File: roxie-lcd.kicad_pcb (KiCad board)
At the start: 2 copper layers, 7 parts, among them J1 Arduino-NANO-33, J2 VESC, J3 TFT, J4 BUTTON_1, J5 BUTTON_2, J6 BUTTON_3, J7 SD

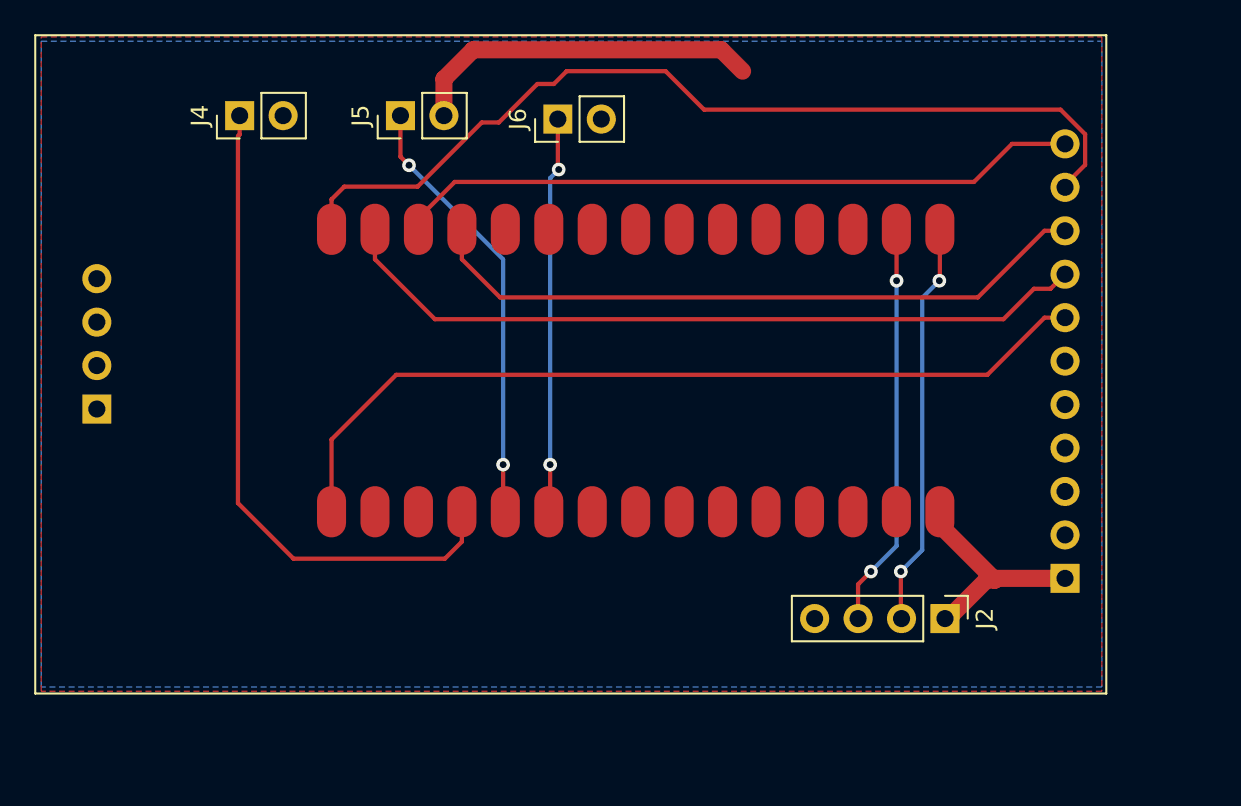
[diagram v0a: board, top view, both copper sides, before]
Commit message: changed button position
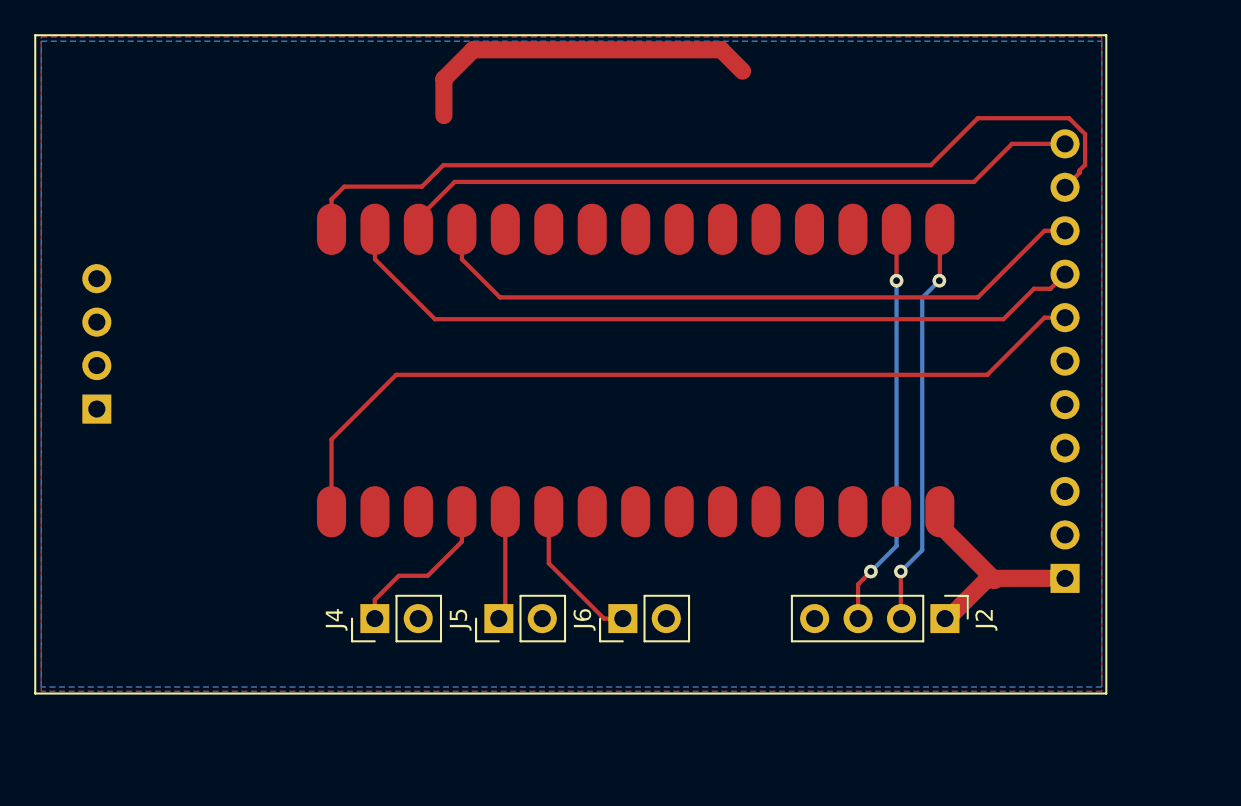
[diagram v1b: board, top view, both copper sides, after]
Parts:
- moved J4 30.4 mm to (45.2, 59.5)
- moved J5 30.0 mm to (52.5, 59.5)
- moved J6 29.4 mm to (59.8, 59.5)
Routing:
- net BUTTON_1: track 39.3 -> 9.35 mm
- net BUTTON_2: track 25.7 -> 6.40 mm, vias 2 -> 0
- net BUTTON_3: track 23.2 -> 8.68 mm, vias 2 -> 0
- net RST: track 54.2 -> 51.7 mm
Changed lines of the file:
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@@
     (thickness 1.6)
     (drawings 4)
-    (tracks 88)
+    (tracks 72)
     (zones 0)
     (modules 7)
@@
   )
   (setup
-    (last_trace_width 1)
+    (last_trace_width 0.25)
     (user_trace_width 1)
     (trace_clearance 0.2)
@@
   )
   (module Connector_PinHeader_2.54mm:PinHeader_1x02_P2.54mm_Vertical (layer F.Cu)
-    (at 55.95 30.3 90)
+    (at 59.75 59.5 90)
     (descr "Through hole straight pin header, 1x02, 2.54mm pitch, single row")
     (tags "Through hole pin header THT 1x02 2.54mm single row")
@@
   )
   (module Connector_PinHeader_2.54mm:PinHeader_1x02_P2.54mm_Vertical (layer F.Cu)
-    (at 46.75 30.1 90)
+    (at 52.5 59.5 90)
     (descr "Through hole straight pin header, 1x02, 2.54mm pitch, single row")
     (tags "Through hole pin header THT 1x02 2.54mm single row")
@@
   )
   (module Connector_PinHeader_2.54mm:PinHeader_1x02_P2.54mm_Vertical (layer F.Cu)
-    (at 37.35 30.1 90)
+    (at 45.25 59.5 90)
     (descr "Through hole straight pin header, 1x02, 2.54mm pitch, single row")
     (tags "Through hole pin header THT 1x02 2.54mm single row")
@@
   (segment (start 45.26 38.495) (end 45.26 36.745) (width 0.25) (layer F.Cu) (net 23))
   (segment (start 82 42) (end 48.765 42) (width 0.25) (layer F.Cu) (net 23))
-  (segment (start 85.598 34.29) (end 85.46 34.29) (width 0.25) (layer F.Cu) (net 24))
-  (segment (start 86.773001 31.185999) (end 85.337002 29.75) (width 0.25) (layer F.Cu) (net 24))
-  (segment (start 85.46 34.29) (end 86.773001 32.976999) (width 0.25) (layer F.Cu) (net 24))
+  (segment (start 86.447999 33.440001) (end 86.447999 33.302001) (width 0.25) (layer F.Cu) (net 24))
+  (segment (start 85.598 34.29) (end 86.447999 33.440001) (width 0.25) (layer F.Cu) (net 24))
+  (segment (start 86.773001 31.185999) (end 85.837002 30.25) (width 0.25) (layer F.Cu) (net 24))
+  (segment (start 86.447999 33.302001) (end 86.773001 32.976999) (width 0.25) (layer F.Cu) (net 24))
   (segment (start 86.773001 32.976999) (end 86.773001 31.185999) (width 0.25) (layer F.Cu) (net 24))
-  (segment (start 85.337002 29.75) (end 64.5 29.75) (width 0.25) (layer F.Cu) (net 24))
-  (segment (start 64.5 29.75) (end 62.25 27.5) (width 0.25) (layer F.Cu) (net 24))
-  (segment (start 56.464998 27.5) (end 55.714998 28.25) (width 0.25) (layer F.Cu) (net 24))
-  (segment (start 62.25 27.5) (end 56.464998 27.5) (width 0.25) (layer F.Cu) (net 24))
-  (segment (start 55.714998 28.25) (end 54.75 28.25) (width 0.25) (layer F.Cu) (net 24))
-  (segment (start 54.75 28.25) (end 52.5 30.5) (width 0.25) (layer F.Cu) (net 24))
-  (segment (start 52.5 30.5) (end 51.5 30.5) (width 0.25) (layer F.Cu) (net 24))
-  (segment (start 51.5 30.5) (end 47.75 34.25) (width 0.25) (layer F.Cu) (net 24))
+  (segment (start 85.837002 30.25) (end 80.5 30.25) (width 0.25) (layer F.Cu) (net 24))
+  (segment (start 80.5 30.25) (end 77.75 33) (width 0.25) (layer F.Cu) (net 24))
+  (segment (start 77.75 33) (end 49.25 33) (width 0.25) (layer F.Cu) (net 24))
+  (segment (start 49.25 33) (end 48 34.25) (width 0.25) (layer F.Cu) (net 24))
   (segment (start 43.465 34.25) (end 42.72 34.995) (width 0.25) (layer F.Cu) (net 24))
   (segment (start 42.72 34.995) (end 42.72 36.745) (width 0.25) (layer F.Cu) (net 24))
-  (segment (start 47.75 34.25) (end 43.465 34.25) (width 0.25) (layer F.Cu) (net 24))
+  (segment (start 48 34.25) (end 43.465 34.25) (width 0.25) (layer F.Cu) (net 24))
   (segment (start 78.28 53.255) (end 78.28 54.03) (width 1) (layer F.Cu) (net 25))
   (segment (start 78.28 54.03) (end 81.5 57.25) (width 1) (layer F.Cu) (net 25))
@@
   (segment (start 81 57.25) (end 81.5 57.25) (width 1) (layer F.Cu) (net 25))
   (segment (start 78.75 59.5) (end 81 57.25) (width 1) (layer F.Cu) (net 25))
-  (via (at 56 33.25) (size 0.8) (drill 0.4) (layers F.Cu B.Cu) (net 26))
-  (segment (start 55.95 30.3) (end 55.95 33.2) (width 0.25) (layer F.Cu) (net 26))
-  (segment (start 55.95 33.2) (end 56 33.25) (width 0.25) (layer F.Cu) (net 26))
-  (via (at 55.5 50.5) (size 0.8) (drill 0.4) (layers F.Cu B.Cu) (net 26))
-  (segment (start 56 33.25) (end 55.5 33.75) (width 0.25) (layer B.Cu) (net 26))
-  (segment (start 55.5 33.75) (end 55.5 50.5) (width 0.25) (layer B.Cu) (net 26))
-  (segment (start 55.5 53.175) (end 55.42 53.255) (width 0.25) (layer F.Cu) (net 26))
-  (segment (start 55.5 50.5) (end 55.5 53.175) (width 0.25) (layer F.Cu) (net 26))
-  (segment (start 50.34 55.005) (end 50.34 53.255) (width 0.25) (layer F.Cu) (net 27))
-  (segment (start 37.35 30.1) (end 37.35 31.2) (width 0.25) (layer F.Cu) (net 27))
-  (segment (start 49.345 56) (end 50.34 55.005) (width 0.25) (layer F.Cu) (net 27))
-  (segment (start 37.25 31.3) (end 37.25 52.75) (width 0.25) (layer F.Cu) (net 27))
-  (segment (start 37.25 52.75) (end 40.5 56) (width 0.25) (layer F.Cu) (net 27))
-  (segment (start 40.5 56) (end 49.345 56) (width 0.25) (layer F.Cu) (net 27))
-  (segment (start 37.35 31.2) (end 37.25 31.3) (width 0.25) (layer F.Cu) (net 27))
+  (segment (start 58.65 59.5) (end 59.75 59.5) (width 0.25) (layer F.Cu) (net 26))
+  (segment (start 55.42 56.27) (end 58.65 59.5) (width 0.25) (layer F.Cu) (net 26))
+  (segment (start 55.42 53.255) (end 55.42 56.27) (width 0.25) (layer F.Cu) (net 26))
+  (segment (start 50.34 55.005) (end 48.345 57) (width 0.25) (layer F.Cu) (net 27))
+  (segment (start 50.34 53.255) (end 50.34 55.005) (width 0.25) (layer F.Cu) (net 27))
+  (segment (start 45.25 58.4) (end 45.25 59.5) (width 0.25) (layer F.Cu) (net 27))
+  (segment (start 46.65 57) (end 45.25 58.4) (width 0.25) (layer F.Cu) (net 27))
+  (segment (start 48.345 57) (end 46.65 57) (width 0.25) (layer F.Cu) (net 27))
   (segment (start 66.75 27.5) (end 65.5 26.25) (width 1) (layer F.Cu) (net 28))
   (segment (start 65.5 26.25) (end 51 26.25) (width 1) (layer F.Cu) (net 28))
@@
   (segment (start 42.72 49.03) (end 42.72 53.255) (width 0.25) (layer F.Cu) (net 29))
   (segment (start 46.5 45.25) (end 42.72 49.03) (width 0.25) (layer F.Cu) (net 29))
-  (segment (start 46.75 30.1) (end 46.75 32.5) (width 0.25) (layer F.Cu) (net 30))
-  (via (at 47.25 33) (size 0.8) (drill 0.4) (layers F.Cu B.Cu) (net 30))
-  (segment (start 46.75 32.5) (end 47.25 33) (width 0.25) (layer F.Cu) (net 30))
-  (via (at 52.75 50.5) (size 0.8) (drill 0.4) (layers F.Cu B.Cu) (net 30))
-  (segment (start 47.25 33) (end 52.75 38.5) (width 0.25) (layer B.Cu) (net 30))
-  (segment (start 52.75 38.5) (end 52.75 50.5) (width 0.25) (layer B.Cu) (net 30))
-  (segment (start 52.75 53.125) (end 52.88 53.255) (width 0.25) (layer F.Cu) (net 30))
-  (segment (start 52.75 50.5) (end 52.75 53.125) (width 0.25) (layer F.Cu) (net 30))
+  (segment (start 52.88 59.12) (end 52.5 59.5) (width 0.25) (layer F.Cu) (net 30))
+  (segment (start 52.88 53.255) (end 52.88 59.12) (width 0.25) (layer F.Cu) (net 30))
   (zone (net 28) (net_name GND) (layer F.Cu) (hatch edge 0.508)
     (connect_pads (clearance 0.508))

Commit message: changed some positions
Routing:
- net TX: track 23.7 -> 23.8 mm, vias 2 -> 1
- net RX: vias 2 -> 1
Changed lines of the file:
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@@
     (thickness 1.6)
     (drawings 4)
-    (tracks 72)
+    (tracks 69)
     (zones 0)
     (modules 7)
@@
   (segment (start 77.25 40.75) (end 77.25 55.5) (width 0.25) (layer B.Cu) (net 19))
   (segment (start 77.25 55.5) (end 76.04 56.71) (width 0.25) (layer B.Cu) (net 19))
-  (via (at 76 56.75) (size 0.8) (drill 0.4) (layers F.Cu B.Cu) (net 19))
   (segment (start 76.04 56.71) (end 76 56.75) (width 0.25) (layer B.Cu) (net 19))
   (segment (start 76 59.46) (end 76.04 59.5) (width 0.25) (layer F.Cu) (net 19))
-  (segment (start 76 56.75) (end 76 59.46) (width 0.25) (layer F.Cu) (net 19))
-  (via (at 74.25 56.75) (size 0.8) (drill 0.4) (layers F.Cu B.Cu) (net 20))
-  (segment (start 73.5 59.5) (end 73.5 57.5) (width 0.25) (layer F.Cu) (net 20))
-  (segment (start 73.5 57.5) (end 74.25 56.75) (width 0.25) (layer F.Cu) (net 20))
+  (segment (start 76.04 56.71) (end 76.04 59.5) (width 0.25) (layer B.Cu) (net 19))
   (via (at 75.75 39.75) (size 0.8) (drill 0.4) (layers F.Cu B.Cu) (net 20))
-  (segment (start 74.25 56.75) (end 75.75 55.25) (width 0.25) (layer B.Cu) (net 20))
-  (segment (start 75.75 55.25) (end 75.75 39.75) (width 0.25) (layer B.Cu) (net 20))
   (segment (start 75.75 36.755) (end 75.74 36.745) (width 0.25) (layer F.Cu) (net 20))
   (segment (start 75.75 39.75) (end 75.75 36.755) (width 0.25) (layer F.Cu) (net 20))
+  (segment (start 75.75 39.75) (end 75.75 55.25) (width 0.25) (layer B.Cu) (net 20))
+  (segment (start 73.5 57.5) (end 73.5 59.5) (width 0.25) (layer B.Cu) (net 20))
+  (segment (start 75.75 55.25) (end 73.5 57.5) (width 0.25) (layer B.Cu) (net 20))
   (segment (start 50.34 38.495) (end 50.34 36.745) (width 0.25) (layer F.Cu) (net 21))
   (segment (start 80.500918 40.725001) (end 52.570001 40.725001) (width 0.25) (layer F.Cu) (net 21))

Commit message: pcb designed
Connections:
- J1 pad 26: Net-(J1-Pad26) -> CS
- J1 pad 28: CS -> Net-(J1-Pad28)
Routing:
- net GND: track 20.8 -> 0.00 mm
- net CS: track 40.2 -> 35.2 mm
- net RST: track 51.7 -> 52.4 mm

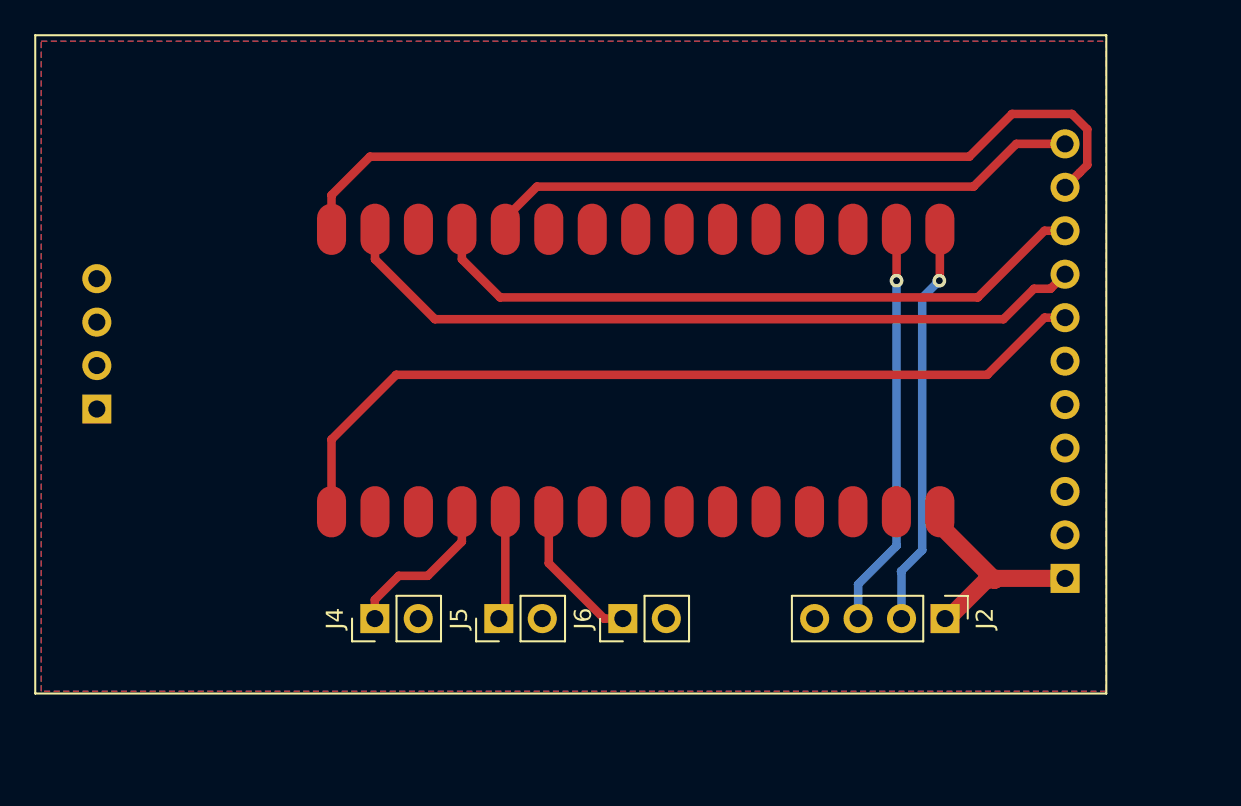
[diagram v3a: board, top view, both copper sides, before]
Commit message: changed position of connectors
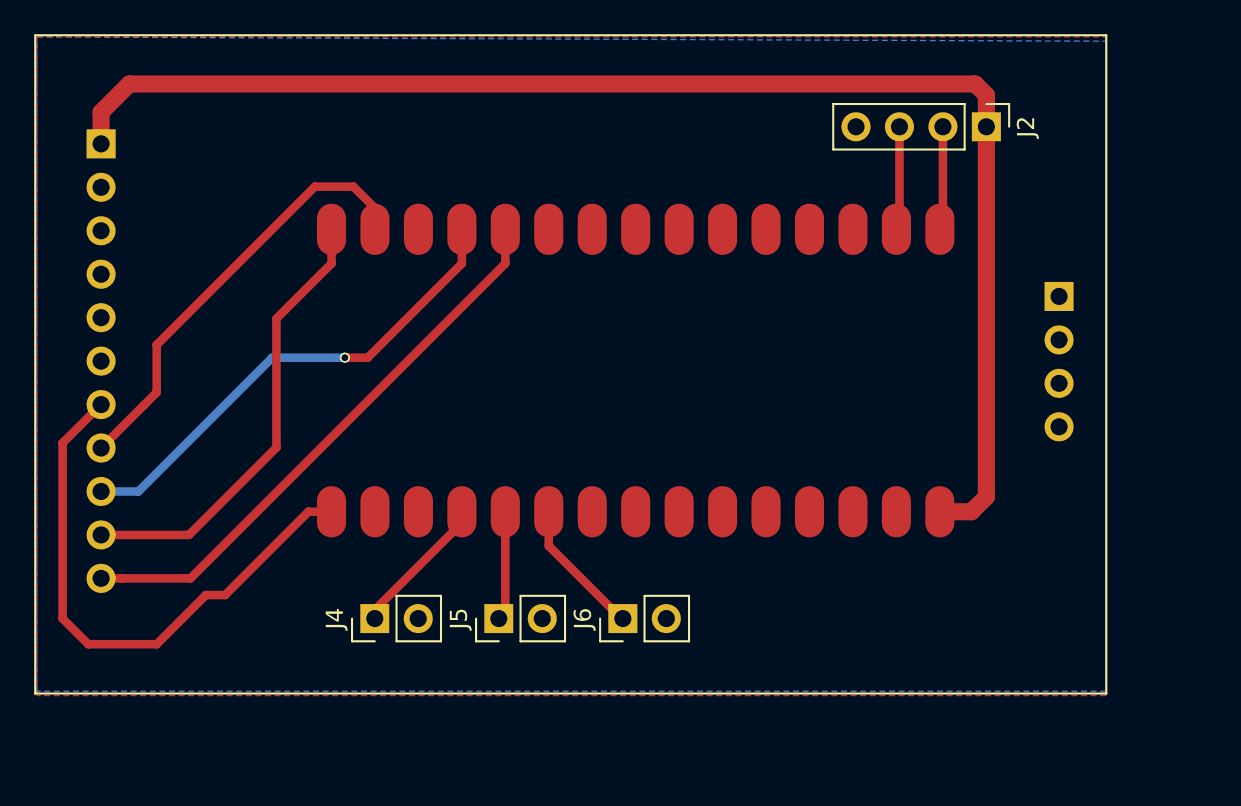
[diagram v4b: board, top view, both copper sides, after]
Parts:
- moved J3 61.8 mm to (29.2, 31.8), turned to 180 degrees
- moved J7 56.6 mm to (85.2, 40.7), turned to 180 degrees
- moved J2 28.9 mm to (81.0, 30.8)
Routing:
- net 5V: track 13.3 -> 81.1 mm
- net RST: track 52.4 -> 26.5 mm
- net SDA: track 44.6 -> 25.7 mm
- net TX: track 23.8 -> 6.07 mm, vias 1 -> 0
- net RX: track 23.7 -> 6.07 mm, vias 1 -> 0
- net CLK: track 50.1 -> 33.0 mm
- net RS: track 39.5 -> 28.6 mm, vias 0 -> 1
- net CS: track 35.2 -> 33.3 mm
- net BUTTON_1: track 9.35 -> 8.35 mm
- net BUTTON_3: track 8.68 -> 8.09 mm

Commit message: first finished version
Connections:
- J1 pad 12: Net-(J1-Pad12) -> 5V
- J1 pad 15: 5V -> Net-(J1-Pad15)
- J1 pad 28: Net-(J1-Pad28) -> RST
- J1 pad 30: RST -> Net-(J1-Pad30)
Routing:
- net GND: track 0.00 -> 77.6 mm, vias 0 -> 15
- net 5V: track 81.1 -> 94.9 mm
- net SDA: track 25.7 -> 22.5 mm
- net RST: track 26.5 -> 28.9 mm, vias 0 -> 1
- net RS: vias 1 -> 0

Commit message: positioning almost correct
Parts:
- J3, J7: moved to F.Cu
- moved J6 13.1 mm to (72.1, 64.0)
- moved J5 10.9 mm to (62.4, 64.0)
- moved J4 8.96 mm to (53.0, 64.0)
- moved J2 7.91 mm to (86.1, 36.8)
- moved J7 7.62 mm to (91.3, 45.3), turned to 0 degrees
- moved J1 6.82 mm to (65.8, 49.3)
- moved J3 5.92 mm to (32.5, 36.7), turned to 0 degrees
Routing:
- net GND: track 77.6 -> 0.00 mm, vias 15 -> 0
- net CLK: track 33.0 -> 18.4 mm, vias 0 -> 1
- net 5V: track 94.9 -> 82.9 mm
- net BUTTON_3: track 8.09 -> 16.0 mm
- net BUTTON_2: track 6.40 -> 8.98 mm
- net CS: track 33.3 -> 35.6 mm
- net RS: track 28.6 -> 30.9 mm
- net SDA: track 22.5 -> 24.8 mm
- net TX: track 6.07 -> 4.25 mm
- net RX: track 6.07 -> 4.25 mm
- net RST: track 28.9 -> 29.8 mm
- net BUTTON_1: track 8.35 -> 7.54 mm
- removed copper zone on B.Cu, net GND

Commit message: some small adjustments, rotated the sd card connector
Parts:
- moved J7 7.81 mm to (90.0, 53.0), turned to 180 degrees
- moved J3 0.20 mm to (32.5, 36.5)
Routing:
- net CLK: track 18.4 -> 33.2 mm, vias 1 -> 0
